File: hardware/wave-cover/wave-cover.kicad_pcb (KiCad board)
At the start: 2 copper layers, 60 x 60 mm, 11 parts

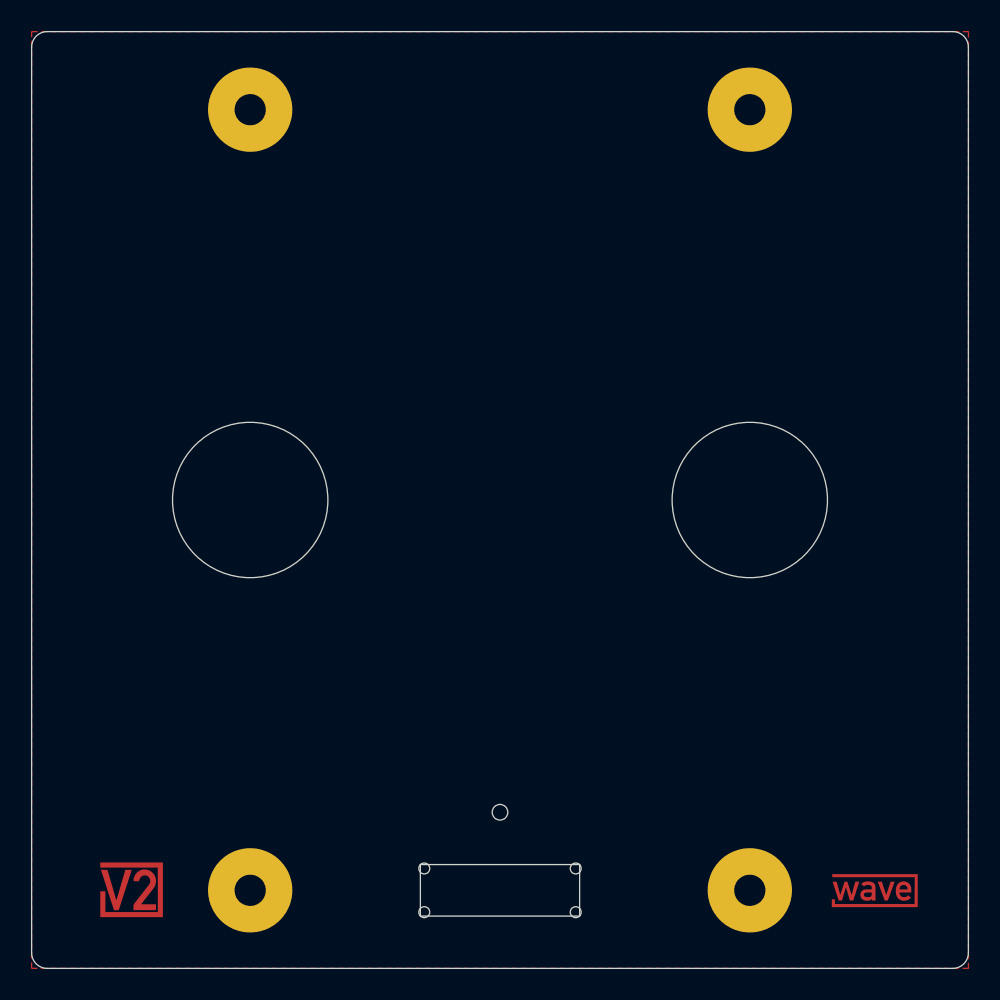
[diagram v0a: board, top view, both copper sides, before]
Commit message: Replace Order_Number
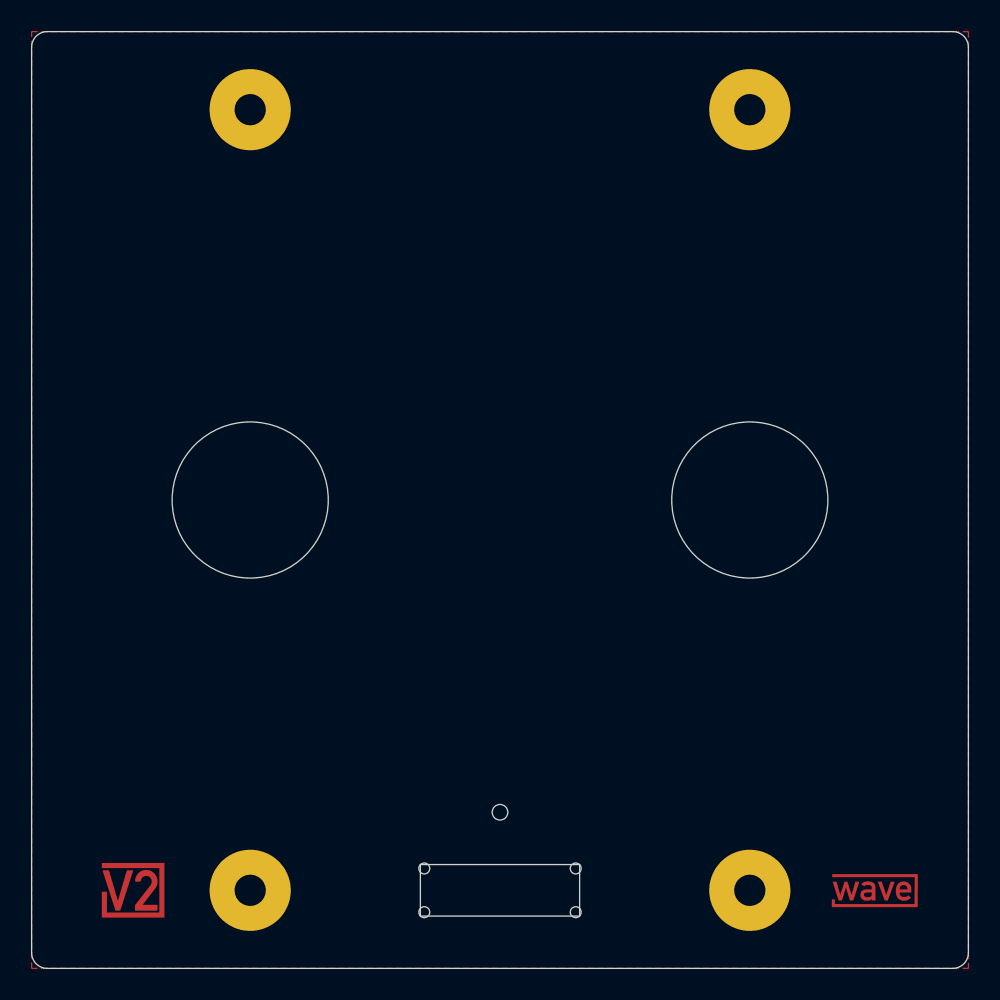
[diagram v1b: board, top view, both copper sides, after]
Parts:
- H101, H102, H103, H104: value MountingHole_2mm_Pad_5.2mm -> 2mm_Pad_5.2mm; footprint V2_Mechanical:Mounting_Hole_2mm_Pad_5.2mm -> V2_Mechanical:MountingHole_2mm_Pad_5.2mm
- H105: value MountingHole_1mm -> 1mm
- H108, H109: value MountingHole_10mm -> 10mm
- INFO101: value ORDER-NUMBER -> ~; footprint V2_Production:Order_Number -> V2_Production:Revision
